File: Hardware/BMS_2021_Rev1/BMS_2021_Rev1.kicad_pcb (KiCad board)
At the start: 2 copper layers, 210.8 x 76.2 mm, 120 parts, among them Q1 2N7002PW, Q2 IRFS7530TRL7PP, Q3 IRFS7530TRL7PP, Q4 2N7002, Q5 2N7002PW, SW1 Relay_SPST, U1 TM4C129E_Launchpad, U2 ACS759ECB-200B-PFF-T, U3 TL3474ACPWR, U4 TL3474ACPWR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

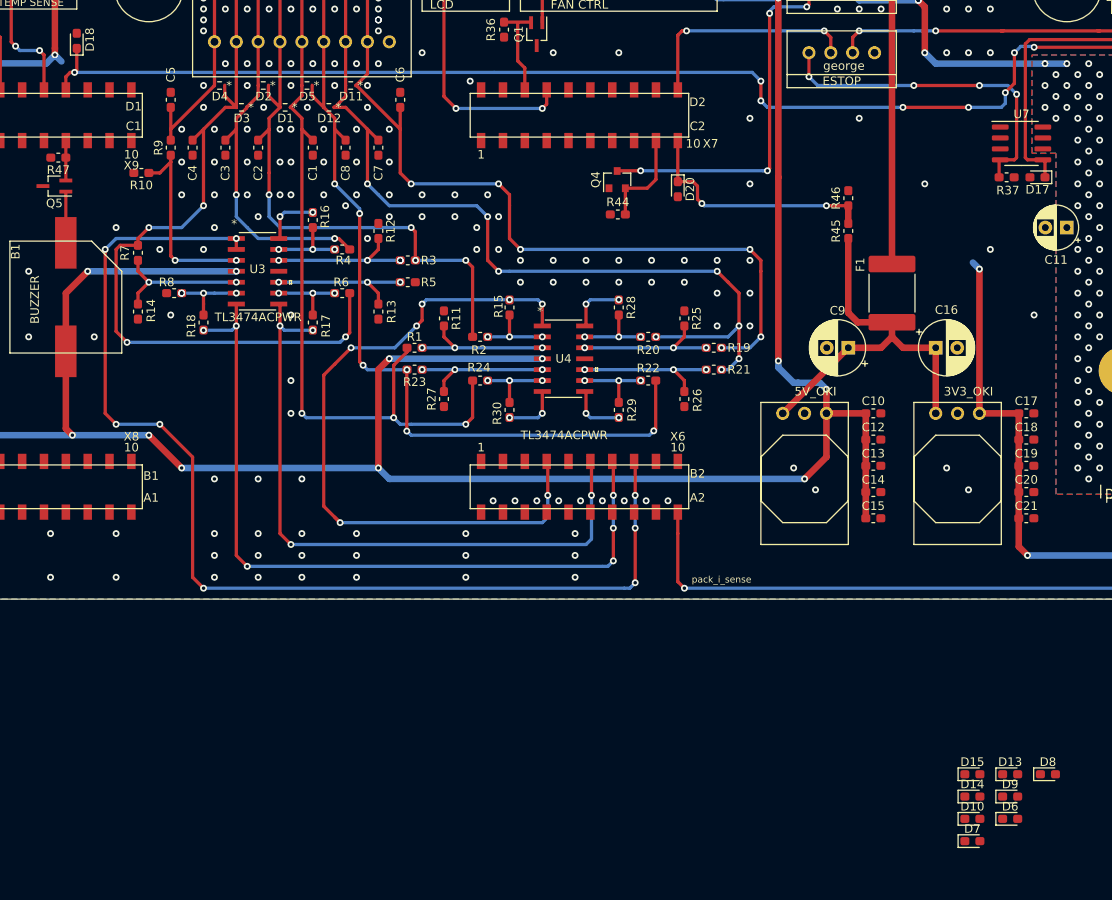
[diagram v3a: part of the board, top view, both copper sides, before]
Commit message: connected the secon +3v3 to tiva, began adding zener diodes
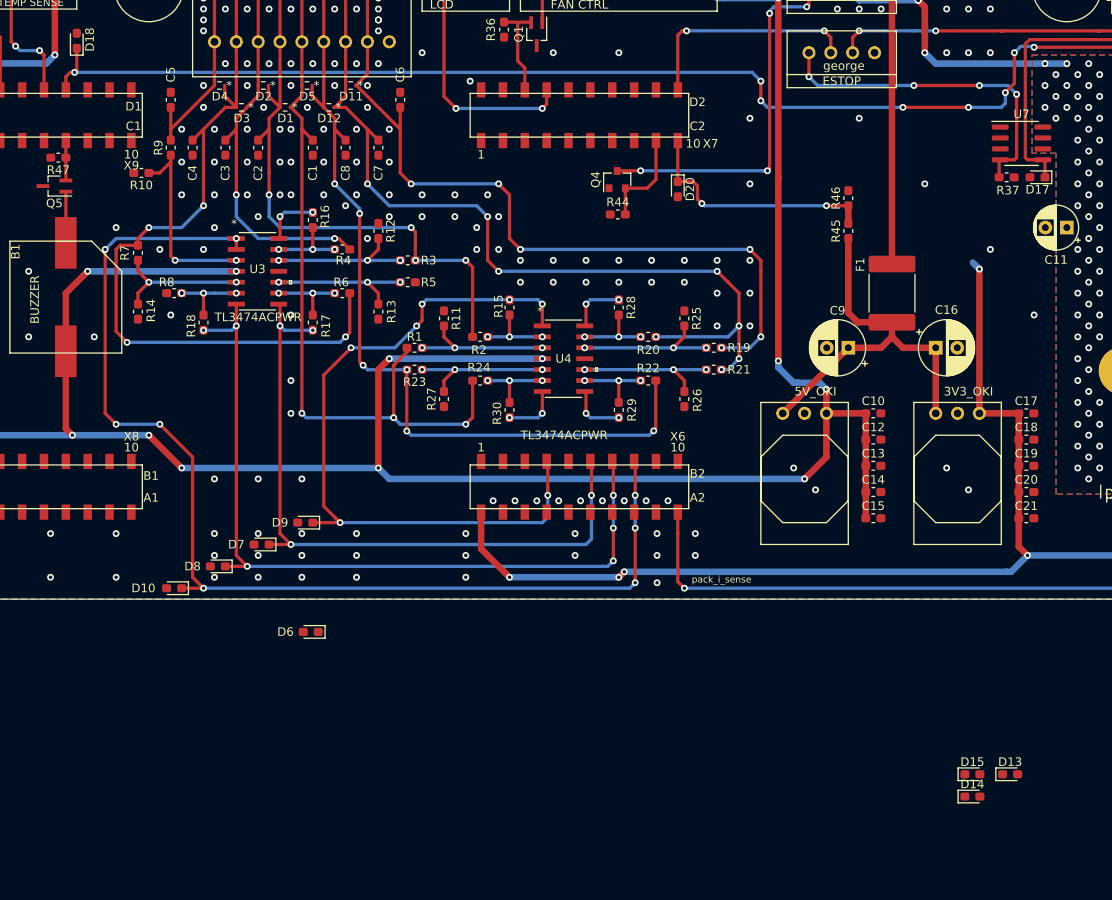
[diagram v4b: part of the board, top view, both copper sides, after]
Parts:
- moved D8 99.4 mm to (95.6, 97.8), turned to 180 degrees
- moved D10 96.6 mm to (90.6, 100.3), turned to 180 degrees
- moved D7 89.5 mm to (100.7, 95.2), turned to 180 degrees
- moved D9 87.9 mm to (105.8, 92.7), turned to 180 degrees
- moved D6 84.1 mm to (106.4, 105.4), turned to 180 degrees
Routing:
- net +3V3: track 211.5 -> 280.6 mm, vias 9 -> 12
- net /cell_5_sense: track 82.7 -> 85.9 mm
- net /cell_3_sense: track 77.2 -> 79.7 mm
- net /cell_2_sense: track 89.4 -> 92.0 mm
- net /cell_1_sense: track 128.8 -> 131.3 mm
- net GND: vias 185 -> 189

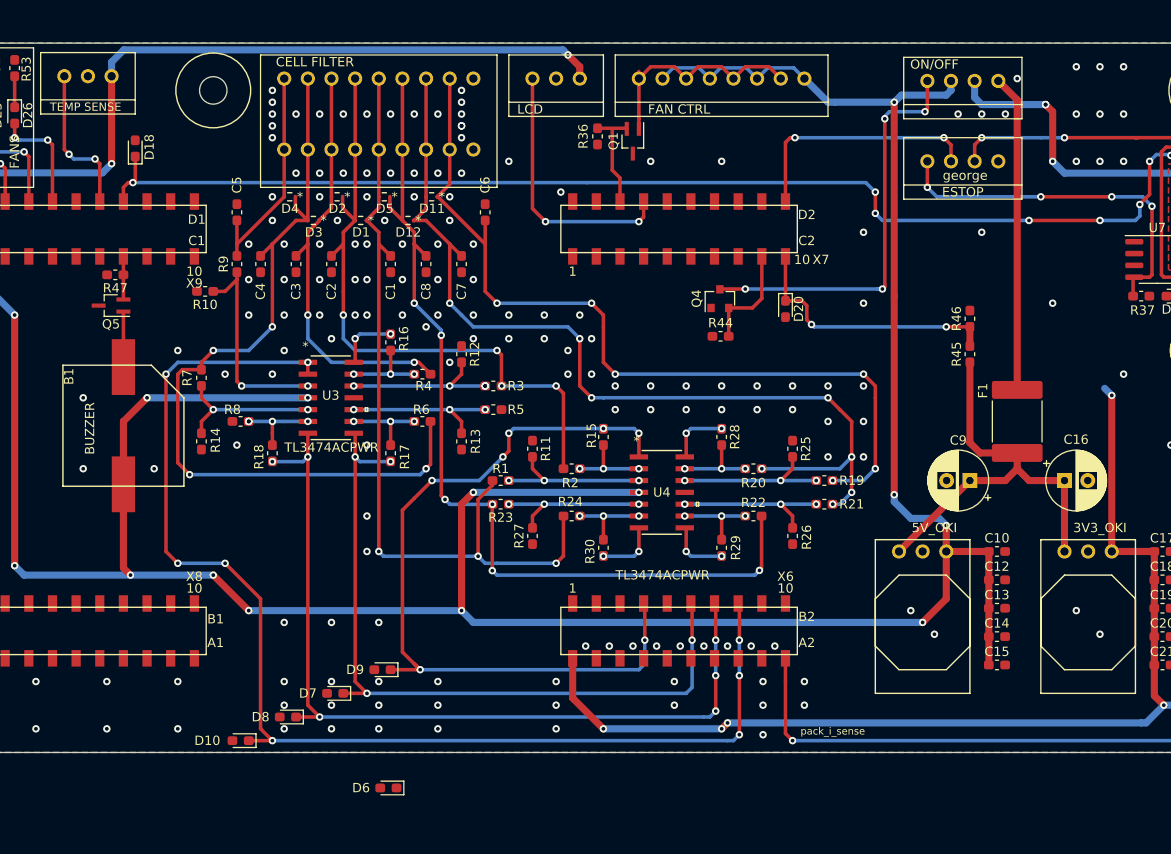
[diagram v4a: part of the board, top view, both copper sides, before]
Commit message: routed 3v3 to top of board, added more diodes.
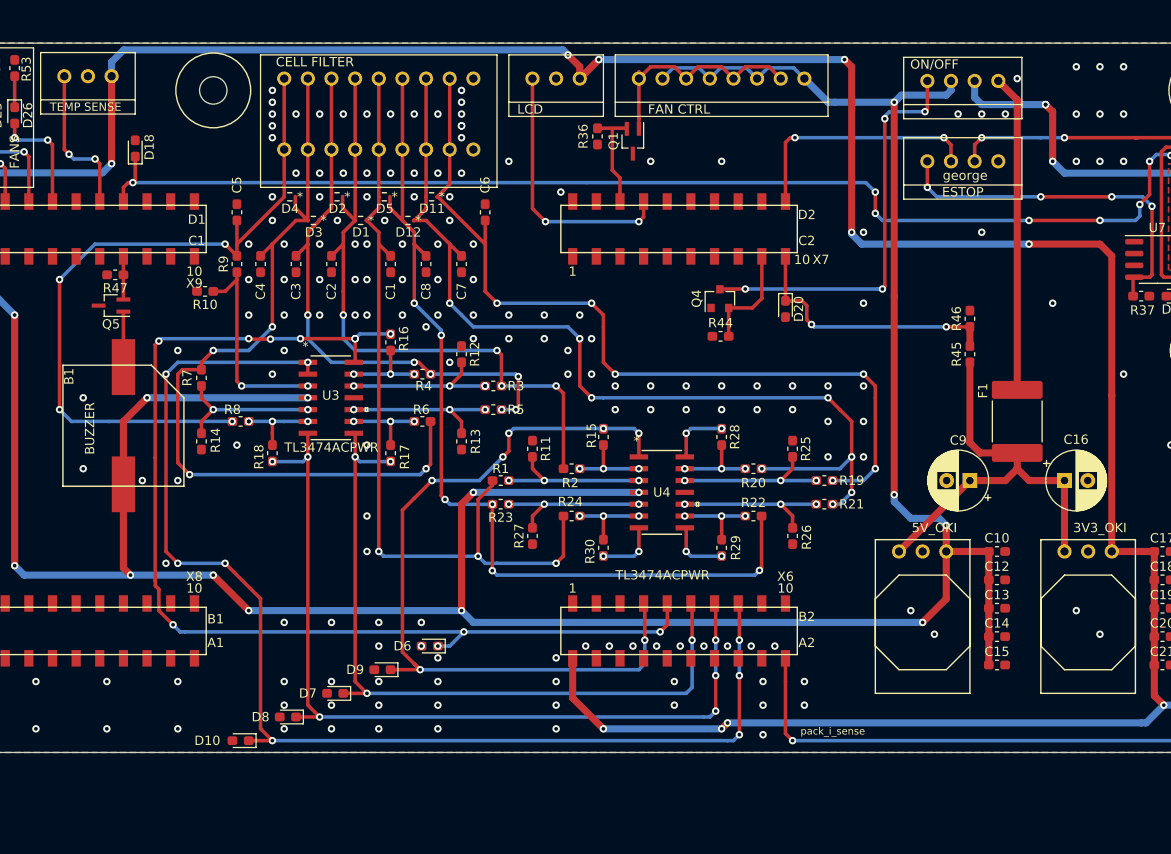
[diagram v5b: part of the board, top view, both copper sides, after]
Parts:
- moved D6 15.9 mm to (110.9, 90.2)
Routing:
- net /cell_4_sense: track 6.62 -> 118.7 mm, vias 2 -> 11
- net +3V3: track 280.6 -> 371.8 mm, vias 12 -> 15
- net /cell_1: track 23.7 -> 77.9 mm, vias 0 -> 4
- net /cell_3: track 45.5 -> 60.3 mm, vias 2 -> 6
- net GND: vias 189 -> 194

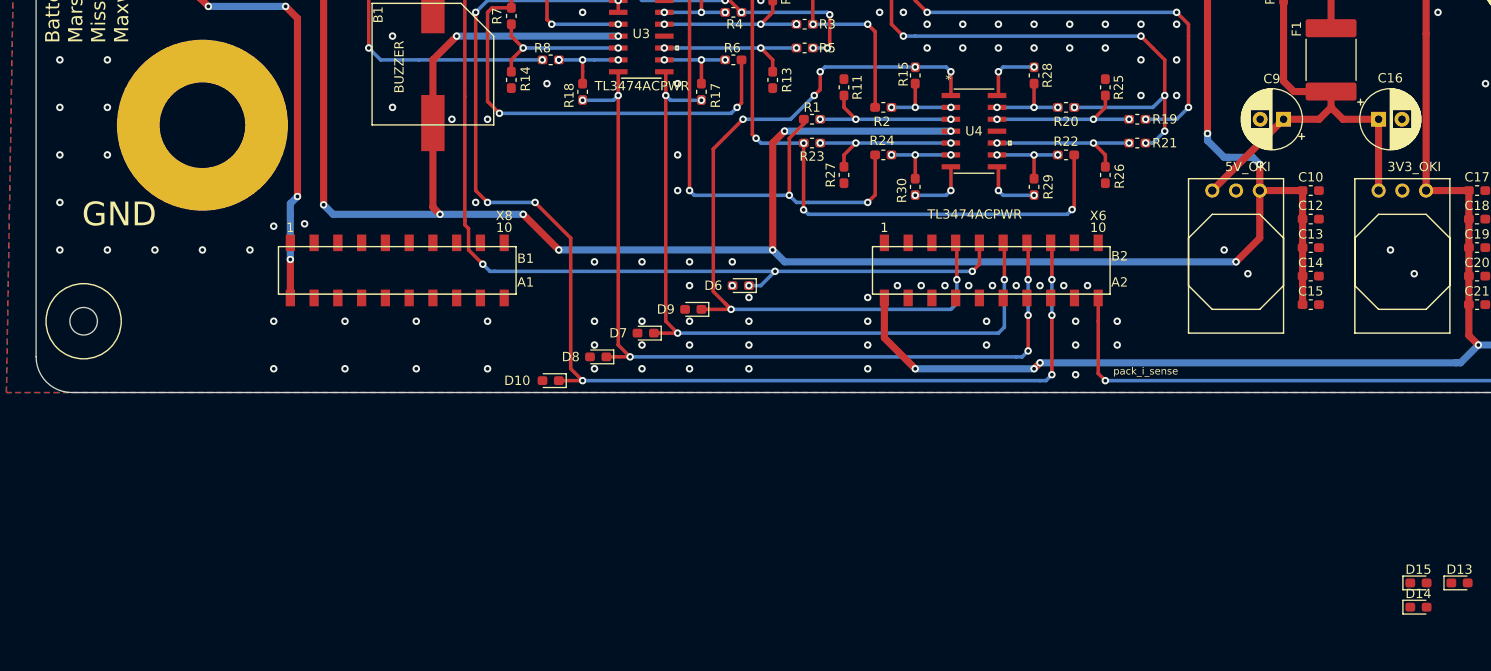
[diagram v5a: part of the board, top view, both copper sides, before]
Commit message: connected more cellFilter zeners
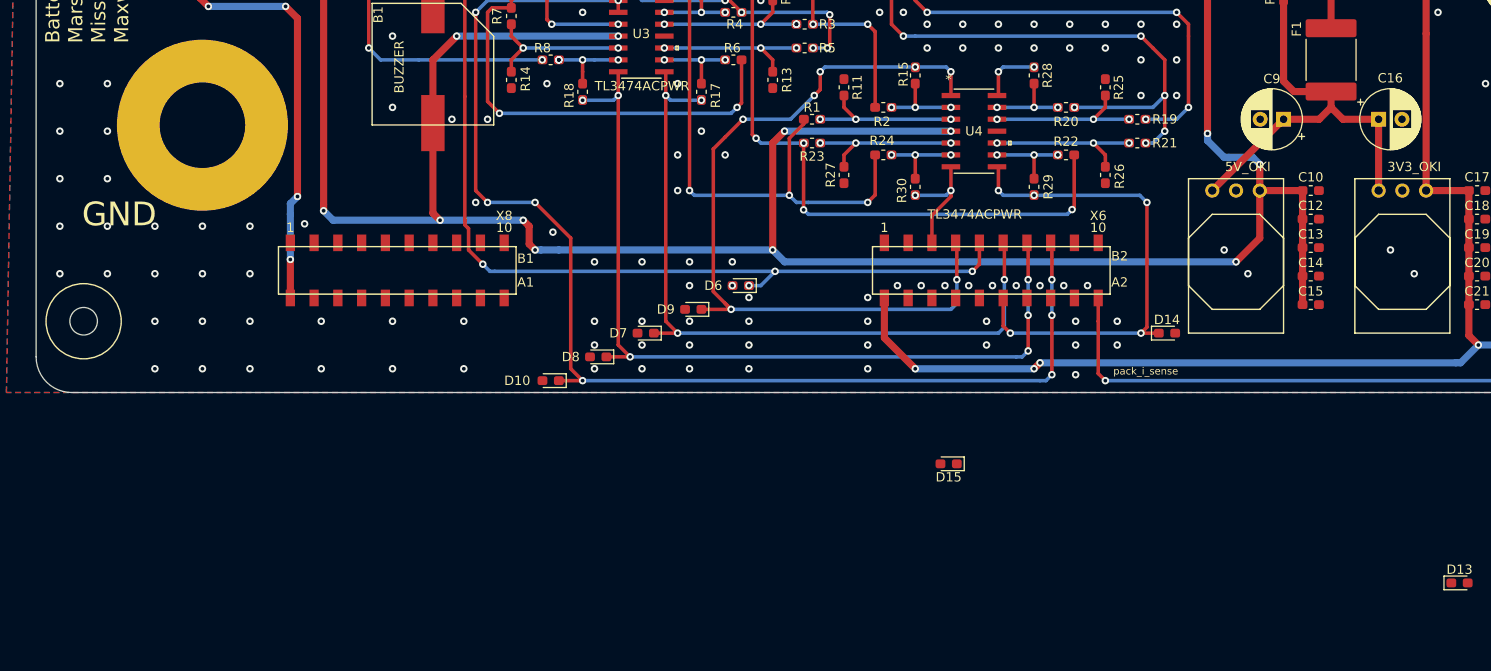
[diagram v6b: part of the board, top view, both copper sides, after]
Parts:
- moved D15 51.8 mm to (133.1, 109.2), turned to 180 degrees
- moved D14 39.8 mm to (156.4, 95.2)
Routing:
- net /cell_7_sense: track 6.62 -> 53.2 mm, vias 2 -> 5
- net /cell_6_sense: track 6.56 -> 13.0 mm
- net +5V: track 345.5 -> 347.6 mm
- net GND: vias 194 -> 204

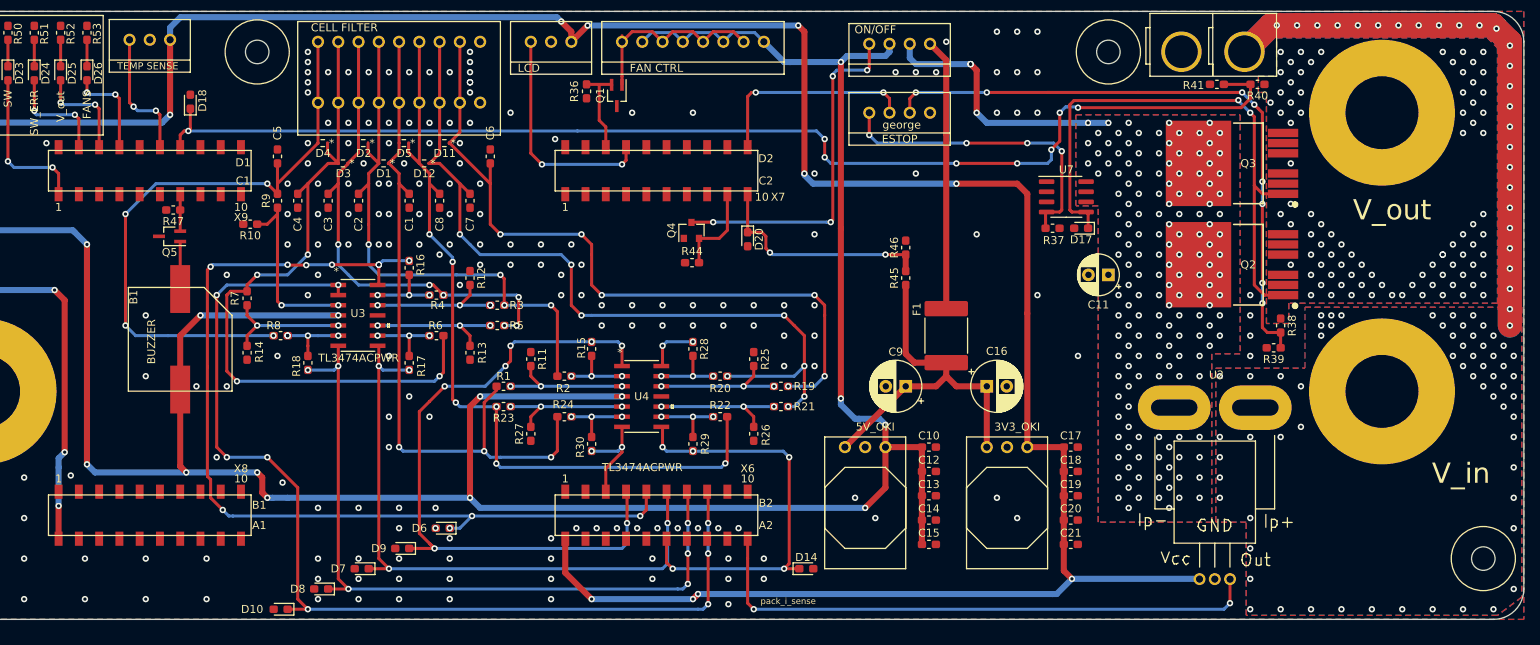
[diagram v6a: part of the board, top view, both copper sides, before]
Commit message: redrew lines for cell 7 and 8 to make to make room to move line 6 (maybe 5 too) for better gnding
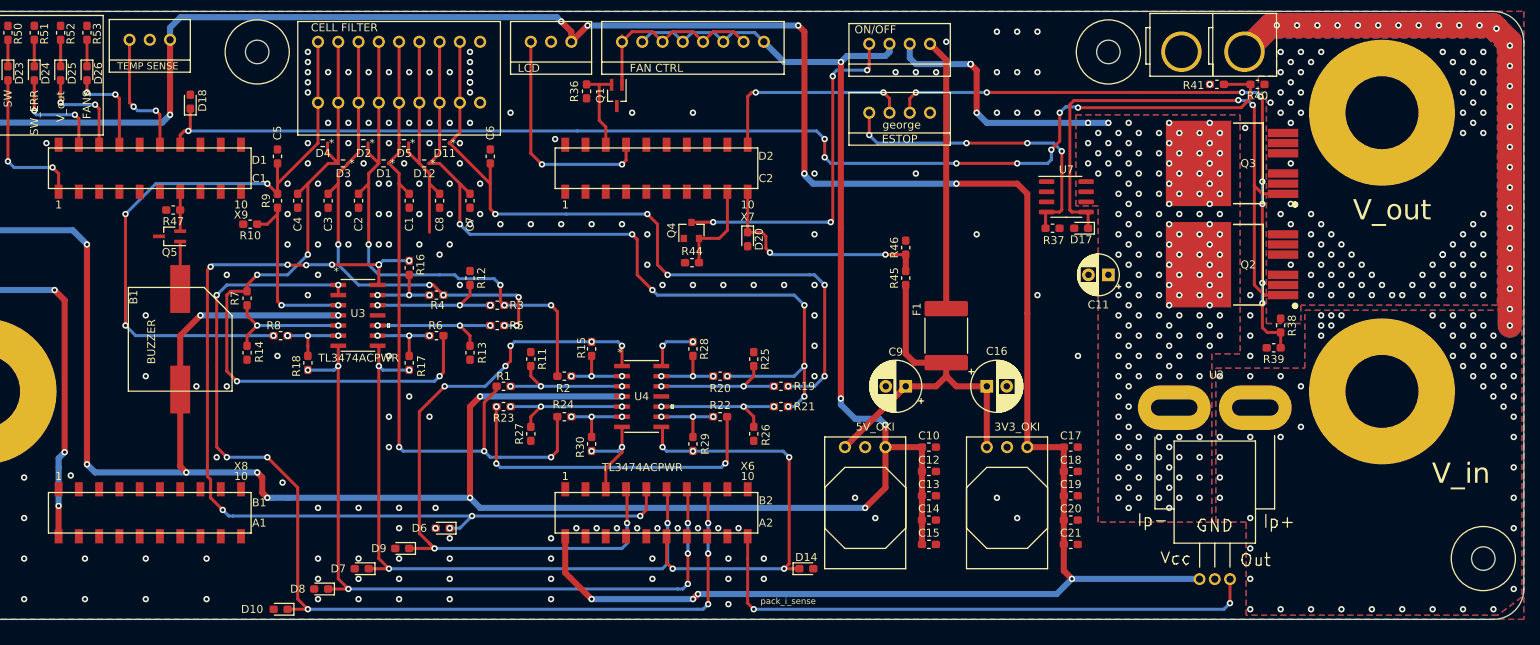
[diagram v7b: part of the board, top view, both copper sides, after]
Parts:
- moved U1 0.30 mm to (61.5, 90.8)
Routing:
- net /cell_6: track 100.0 -> 72.2 mm, vias 6 -> 3
- net /cell_7: track 100.7 -> 101.8 mm
- net Net-(Conn5-Pad3): track 79.2 -> 80.3 mm
- net E_STOP_GATE: track 71.0 -> 71.8 mm
- net /cell_4: track 69.5 -> 68.7 mm
- net GND: vias 204 -> 194
